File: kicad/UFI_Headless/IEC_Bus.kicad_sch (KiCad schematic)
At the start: 7 parts, among them J8 IEC, U10 74LVC14AD, U9 SN74LS07D

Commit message: UFI Headless: 4-layer layout v0.1, LCSC sourcing, fab outputs
- build_pcb.py: footprints from the schematic netlist (KIID-linked), placement,
  pre-routed USB-C fan-out and MCU VSS stubs, In1 GND plane
- make_pcb.sh: Freerouting 2.4.1 routing, violation cleanup, supply widening,
  GND/3V3 pours, stitching vias; DRC 0 errors, schematic parity clean
- LCSC part numbers via JLCPCB API; crystal X322525MOB4SI (CL 12pF, 2x 18pF)
- fertigung/: Gerber, Excellon, BOM/CPL (KiCad + JLC format)

Co-Authored-By: Claude Opus 5.5 <noreply@anthropic.com>
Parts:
- C44, C45: LCSC (none) -> C14663
- RN7, RN8: LCSC (none) -> C20197
- U10: LCSC (none) -> C133541; MPN SN74LVC14AD -> SN74LVC14ADR
- U9: LCSC (none) -> C371970; MPN SN74LS07D (alt. SN7407D) -> SN74LS07DR (alt. SN7407DR)

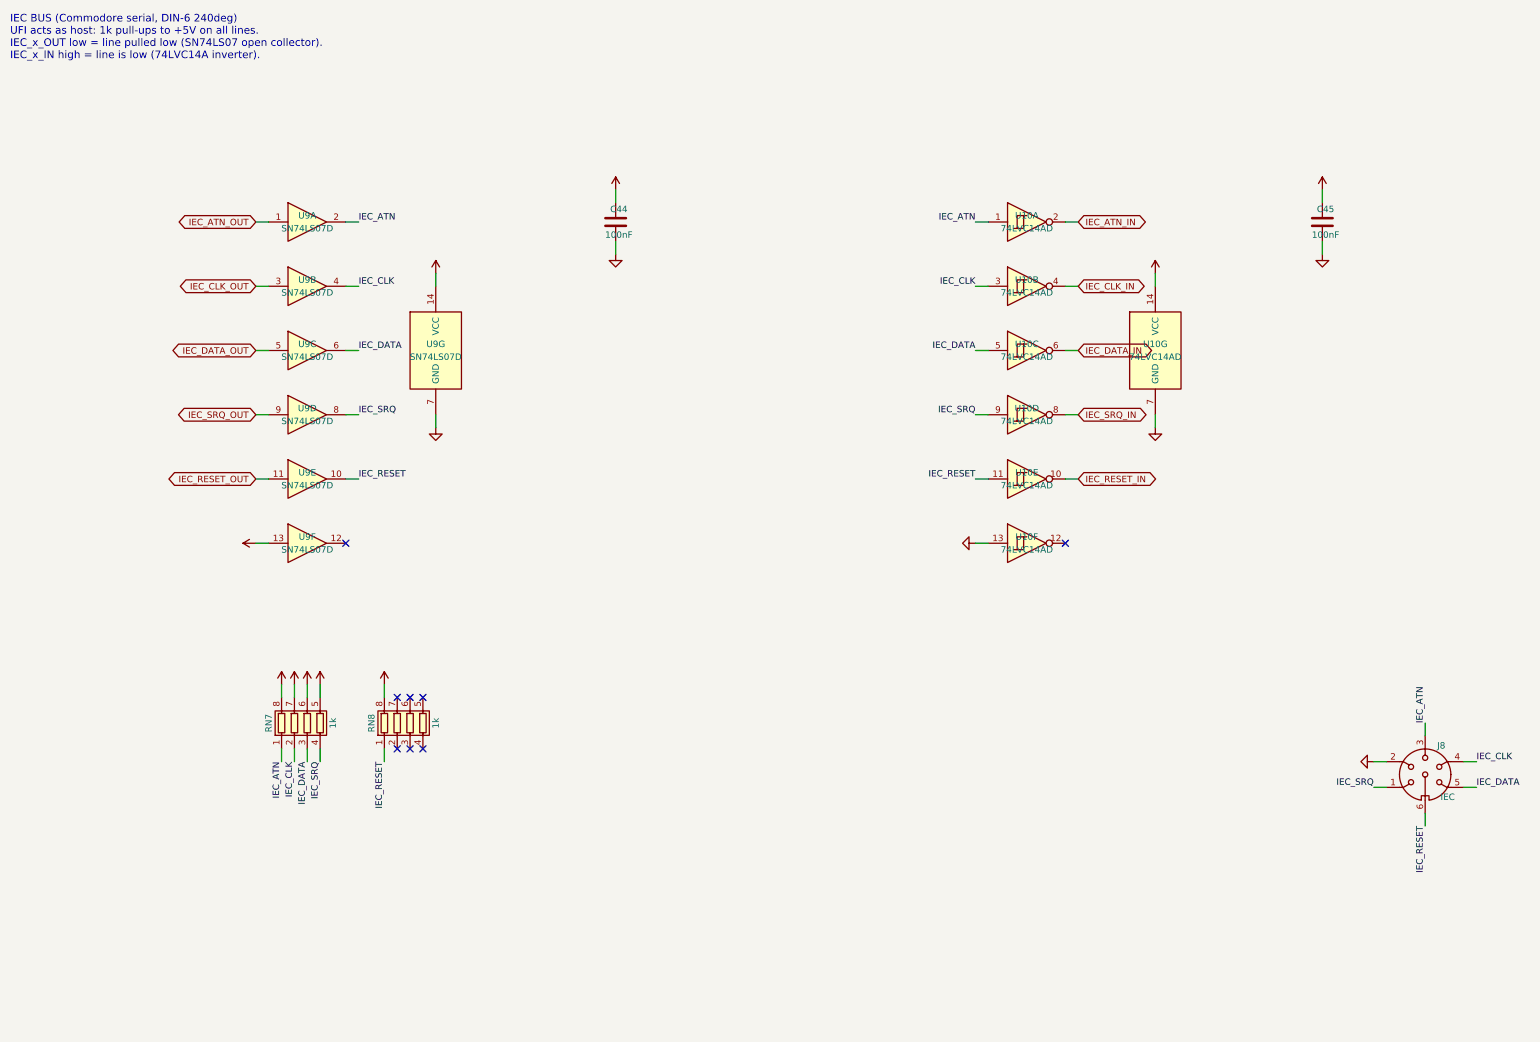
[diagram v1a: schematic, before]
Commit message: UFI Headless: replace on-board DIN-6 with 1x6 IEC header (DIN socket external)
J8 is now a 2.54 mm 1x6 pin header (pin n = DIN-6 pin n, LCSC C37208).
Footprint swapped on the routed board, IEC nets re-routed, IEC_SRQ
U9-U10 hand-routed on In2. DRC: 0 errors, 0 unconnected, parity clean.
Firmware unaffected (MCU pins unchanged). Fab outputs and renders regenerated.

Co-Authored-By: Claude Opus 5.5 <noreply@anthropic.com>
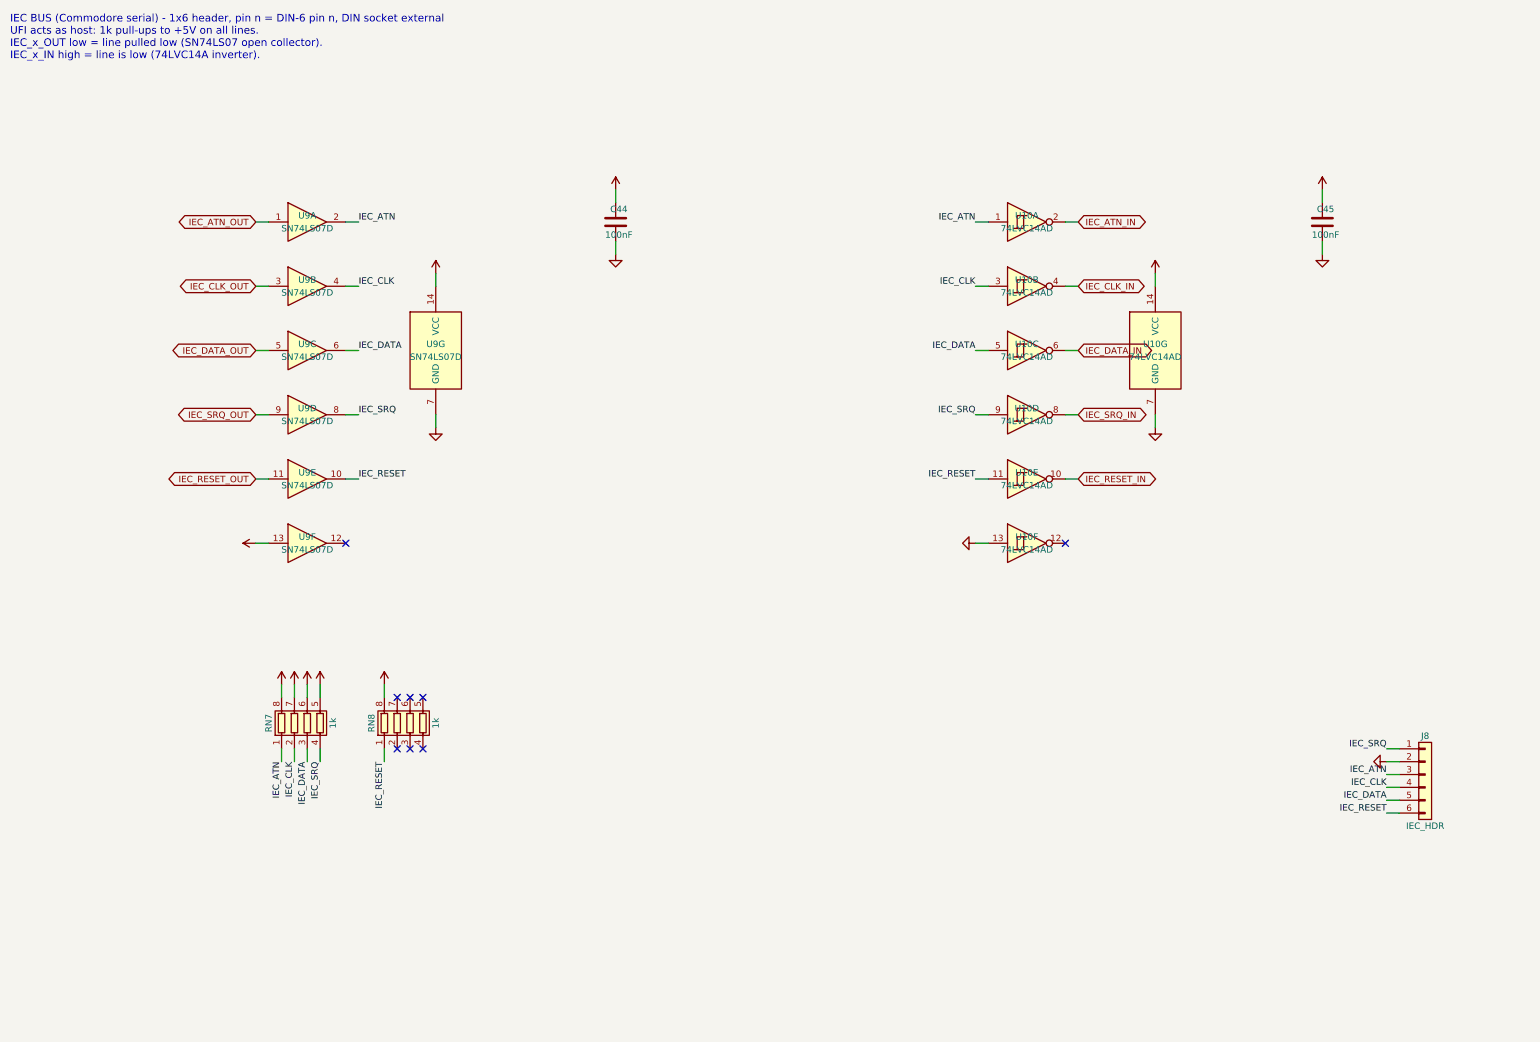
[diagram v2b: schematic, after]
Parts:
- J8: value IEC -> IEC_HDR; footprint UFI:DIN-6_Female_PCB -> Connector_PinHeader_2.54mm:PinHeader_1x06_P2.54mm_Vertical; symbol Connector:DIN-6 -> Connector_Generic:Conn_01x06; LCSC (none) -> C37208; Note 1 SRQ, 2 GND, 3 ATN, 4 CLK, 5 DATA, 6 RESET; footprint to v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 -> Pin n = DIN-6 pin n (1 SRQ, 2 GND, 3 ATN, 4 CLK, 5 DATA, 6 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
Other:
- note added: "IEC BUS (Commodore serial) - 1x6 header, pin n = DIN-6 pin n, DIN socket external UFI acts as host: 1k pull-ups to +5V on all lines. IEC_x_OUT low = line pulled low (SN74LS07 open collector). IEC_x_IN high = line is low (74LVC14A inverter)."
- note removed: "IEC BUS (Commodore serial, DIN-6 240deg) UFI acts as host: 1k pull-ups to +5V on all lines. IEC_x_OUT low = line pulled low (SN74LS07 open collector). IEC_x_IN high = line is low (74LVC14A inverter)."
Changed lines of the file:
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@@
 (paper "A3")
 (title_block (title "UFI Headless - IEC Bus") (date "2026-10-05") (rev "0.1") (company "UFI Project"))
-(text "IEC BUS (Commodore serial, DIN-6 240deg)\nUFI acts as host: 1k pull-ups to +5V on all lines.\nIEC_x_OUT low = line pulled low (SN74LS07 open collector).\nIEC_x_IN high = line is low (74LVC14A inverter)." (exclude_from_sim no) (at 20 20 0) (effects (font (size 1.5 1.5)) (justify left top)))
+(text "IEC BUS (Commodore serial) - 1x6 header, pin n = DIN-6 pin n, DIN socket external\nUFI acts as host: 1k pull-ups to +5V on all lines.\nIEC_x_OUT low = line pulled low (SN74LS07 open collector).\nIEC_x_IN high = line is low (74LVC14A inverter)." (exclude_from_sim no) (at 20 20 0) (effects (font (size 1.5 1.5)) (justify left top)))
 (wire (pts (xy 71.12 60.96) (xy 68.58 60.96)) (stroke (width 0) (type default)))
 (global_label "IEC_ATN_OUT" (shape bidirectional) (at 68.58 60.96 180) (fields_autoplaced yes) (effects (font (size 1.27 1.27)) (justify right)) (property "Intersheetrefs" "${INTERSHEET_REFS}" (at 68.58 60.96 0) (effects (font (size 1.27 1.27)) (hide yes))))
@@
 (no_connect (at 96.52 154.94))
 (wire (pts (xy 93.98 154.94) (xy 93.98 152.4)) (stroke (width 0) (type default)))
-(wire (pts (xy 292.1 172.72) (xy 289.56 172.72)) (stroke (width 0) (type default)))
-(label "IEC_SRQ" (at 289.56 172.72 180) (fields_autoplaced yes) (effects (font (size 1.27 1.27)) (justify right bottom)))
-(wire (pts (xy 292.1 167.64) (xy 289.56 167.64)) (stroke (width 0) (type default)))
-(wire (pts (xy 299.72 162.56) (xy 299.72 160.02)) (stroke (width 0) (type default)))
-(label "IEC_ATN" (at 299.72 160.02 90) (fields_autoplaced yes) (effects (font (size 1.27 1.27)) (justify left bottom)))
-(wire (pts (xy 307.34 167.64) (xy 309.88 167.64)) (stroke (width 0) (type default)))
-(label "IEC_CLK" (at 309.88 167.64 0) (fields_autoplaced yes) (effects (font (size 1.27 1.27)) (justify left bottom)))
-(wire (pts (xy 307.34 172.72) (xy 309.88 172.72)) (stroke (width 0) (type default)))
-(label "IEC_DATA" (at 309.88 172.72 0) (fields_autoplaced yes) (effects (font (size 1.27 1.27)) (justify left bottom)))
-(wire (pts (xy 299.72 177.8) (xy 299.72 180.34)) (stroke (width 0) (type default)))
-(label "IEC_RESET" (at 299.72 180.34 270) (fields_autoplaced yes) (effects (font (size 1.27 1.27)) (justify right bottom)))
+(wire (pts (xy 294.64 165.1) (xy 292.1 165.1)) (stroke (width 0) (type default)))
+(label "IEC_SRQ" (at 292.1 165.1 180) (fields_autoplaced yes) (effects (font (size 1.27 1.27)) (justify right bottom)))
+(wire (pts (xy 294.64 167.64) (xy 292.1 167.64)) (stroke (width 0) (type default)))
+(wire (pts (xy 294.64 170.18) (xy 292.1 170.18)) (stroke (width 0) (type default)))
+(label "IEC_ATN" (at 292.1 170.18 180) (fields_autoplaced yes) (effects (font (size 1.27 1.27)) (justify right bottom)))
+(wire (pts (xy 294.64 172.72) (xy 292.1 172.72)) (stroke (width 0) (type default)))
+(label "IEC_CLK" (at 292.1 172.72 180) (fields_autoplaced yes) (effects (font (size 1.27 1.27)) (justify right bottom)))
+(wire (pts (xy 294.64 175.26) (xy 292.1 175.26)) (stroke (width 0) (type default)))
+(label "IEC_DATA" (at 292.1 175.26 180) (fields_autoplaced yes) (effects (font (size 1.27 1.27)) (justify right bottom)))
+(wire (pts (xy 294.64 177.8) (xy 292.1 177.8)) (stroke (width 0) (type default)))
+(label "IEC_RESET" (at 292.1 177.8 180) (fields_autoplaced yes) (effects (font (size 1.27 1.27)) (justify right bottom)))
 (symbol (lib_id "74xx:74LS07") (at 78.74 60.96 0) (unit 1)
 (exclude_from_sim no) (in_bom yes) (on_board yes) (dnp no)
@@
 (pin "8")
 (instances (project "UFI_Headless" (path "/dc1b800d-cedf-5627-97f0-e6992ff33669/ed0b61ff-f6bd-56db-b8a4-25dbfb310cbc" (reference "RN8") (unit 1)))))
-(symbol (lib_id "power:GND") (at 289.56 167.64 270) (unit 1)
-(exclude_from_sim no) (in_bom no) (on_board yes) (dnp no)
-(property "Reference" "#PWR210" (at 289.56 167.64 0) (effects (font (size 1.27 1.27)) (hide yes)))
-(property "Value" "GND" (at 289.56 167.64 0) (effects (font (size 1.27 1.27)) (hide yes)))
-(property "Footprint" "" (at 289.56 167.64 0) (effects (font (size 1.27 1.27)) (hide yes)))
-(property "Datasheet" "" (at 289.56 167.64 0) (effects (font (size 1.27 1.27)) (hide yes)))
+(symbol (lib_id "power:GND") (at 292.1 167.64 270) (unit 1)
+(exclude_from_sim no) (in_bom no) (on_board yes) (dnp no)
+(property "Reference" "#PWR210" (at 292.1 167.64 0) (effects (font (size 1.27 1.27)) (hide yes)))
+(property "Value" "GND" (at 292.1 167.64 0) (effects (font (size 1.27 1.27)) (hide yes)))
+(property "Footprint" "" (at 292.1 167.64 0) (effects (font (size 1.27 1.27)) (hide yes)))
+(property "Datasheet" "" (at 292.1 167.64 0) (effects (font (size 1.27 1.27)) (hide yes)))
 (pin "1")
 (instances (project "UFI_Headless" (path "/dc1b800d-cedf-5627-97f0-e6992ff33669/ed0b61ff-f6bd-56db-b8a4-25dbfb310cbc" (reference "#PWR210") (unit 1)))))
-(symbol (lib_id "Connector:DIN-6") (at 299.72 170.18 0) (unit 1)
-(exclude_from_sim no) (in_bom yes) (on_board yes) (dnp no)
-(property "Reference" "J8" (at 302.895 164.465 0) (effects (font (size 1.27 1.27))))
-(property "Value" "IEC" (at 304.165 174.625 0) (effects (font (size 1.27 1.27))))
-(property "Footprint" "UFI:DIN-6_Female_PCB" (at 299.72 170.18 0) (effects (font (size 1.27 1.27)) (hide yes)))
-(property "Datasheet" "http://www.mouser.com/ds/2/18/40_c091_abd_e-75918.pdf" (at 299.72 170.18 0) (effects (font (size 1.27 1.27)) (hide yes)))
-(property "Note" "1 SRQ, 2 GND, 3 ATN, 4 CLK, 5 DATA, 6 RESET; footprint to verify" (at 299.72 170.18 0) (effects (font (size 1.27 1.27)) (hide yes)))
-(pin "1")
-(pin "2")
+(symbol (lib_id "Connector_Generic:Conn_01x06") (at 299.72 170.18 0) (unit 1)
+(exclude_from_sim no) (in_bom yes) (on_board yes) (dnp no)
+(property "Reference" "J8" (at 299.72 162.56 0) (effects (font (size 1.27 1.27))))
+(property "Value" "IEC_HDR" (at 299.72 180.34 0) (effects (font (size 1.27 1.27))))
+(property "Footprint" "Connector_PinHeader_2.54mm:PinHeader_1x06_P2.54mm_Vertical" (at 299.72 170.18 0) (effects (font (size 1.27 1.27)) (hide yes)))
+(property "Datasheet" "" (at 299.72 170.18 0) (effects (font (size 1.27 1.27)) (hide yes)))
+(property "LCSC" "C37208" (at 299.72 170.18 0) (effects (font (size 1.27 1.27)) (hide yes)))
+(property "Note" "Pin n = DIN-6 pin n (1 SRQ, 2 GND, 3 ATN, 4 CLK, 5 DATA, 6 RESET); DIN socket external" (at 299.72 170.18 0) (effects (font (size 1.27 1.27)) (hide yes)))
+(pin "1")
+(pin "2")

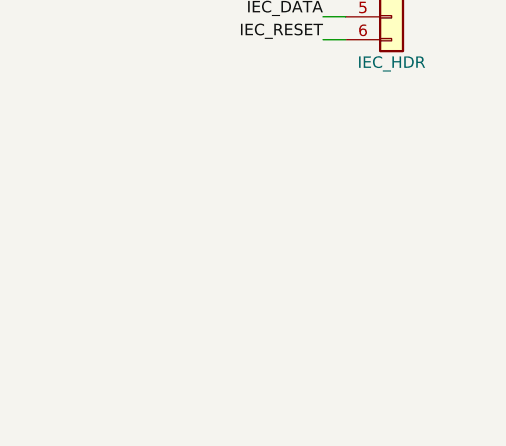
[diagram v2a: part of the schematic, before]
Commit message: UFI Headless v0.2: 8 MB PSRAM, ESD, drive polyfuses, test points
Schematic (new parts get fixed references above the v0.1 maxima, so all
existing references and PCB links stay unchanged):
- U11 APS6404L 8 MB QSPI PSRAM on OCTOSPIM P1 (PB2/PB10/PD11/PD12/PB13/
  PD13), C46, CE# pull-up R16
- D9-D11 ESDA6V1-5SC6 on the 13 Amiga J7 bus lines + MOTOR_A, D12 on IEC
- F2/F3 polyfuses: drive supplies FDD_5V/FDD_12V for J3 and J7 pins 12/23
- TP1-TP6 (3V3, 5V, 12V, GND, RDATA, INDEX), excluded from BOM/CPL
Layout (incremental ECO on the reviewed board):
- scripts/add_parts.py: re-net pads, collision-aware placement, rip up only
  what is in the way; make_pcb.sh 'eco' step
- fixes found on the way: supply pours ran after finish_pcb and left GND
  islands (LDO U4 ground!) without vias -> order swapped, GND pour check
  per net; island/dogbone vias never inside pads; manual_routes no longer
  re-applies the D+ fallback; pipeline filters robust against interleaved
  SWIG noise under pipefail
- DRC rule for the intentional J6/J7 silk overhang instead of warnings;
  netclasses cover the new drive supply nets
DRC: 0 errors, 0 warnings, 0 unconnected, parity clean, no via-in-pad.

Co-Authored-By: Claude Opus 5.5 <noreply@anthropic.com>
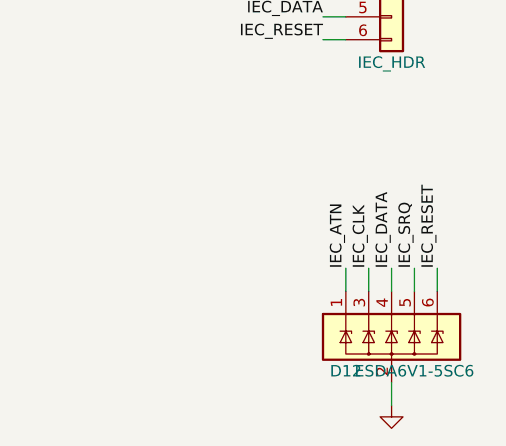
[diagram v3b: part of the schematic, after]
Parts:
- added D12: ESDA6V1-5SC6, Package_TO_SOT_SMD:SOT-23-6, symbol Power_Protection:ESDA6V1-5SC6
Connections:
- net GND: now also D12.2 (GND)
- net IEC_ATN: now also D12.1 (IO1)
- net IEC_CLK: now also D12.3 (IO2)
- net IEC_DATA: now also D12.4 (IO3)
- net IEC_RESET: now also D12.6 (IO5)
- net IEC_SRQ: now also D12.5 (IO4)
